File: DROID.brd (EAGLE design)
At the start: 160 x 100 mm, 83 parts

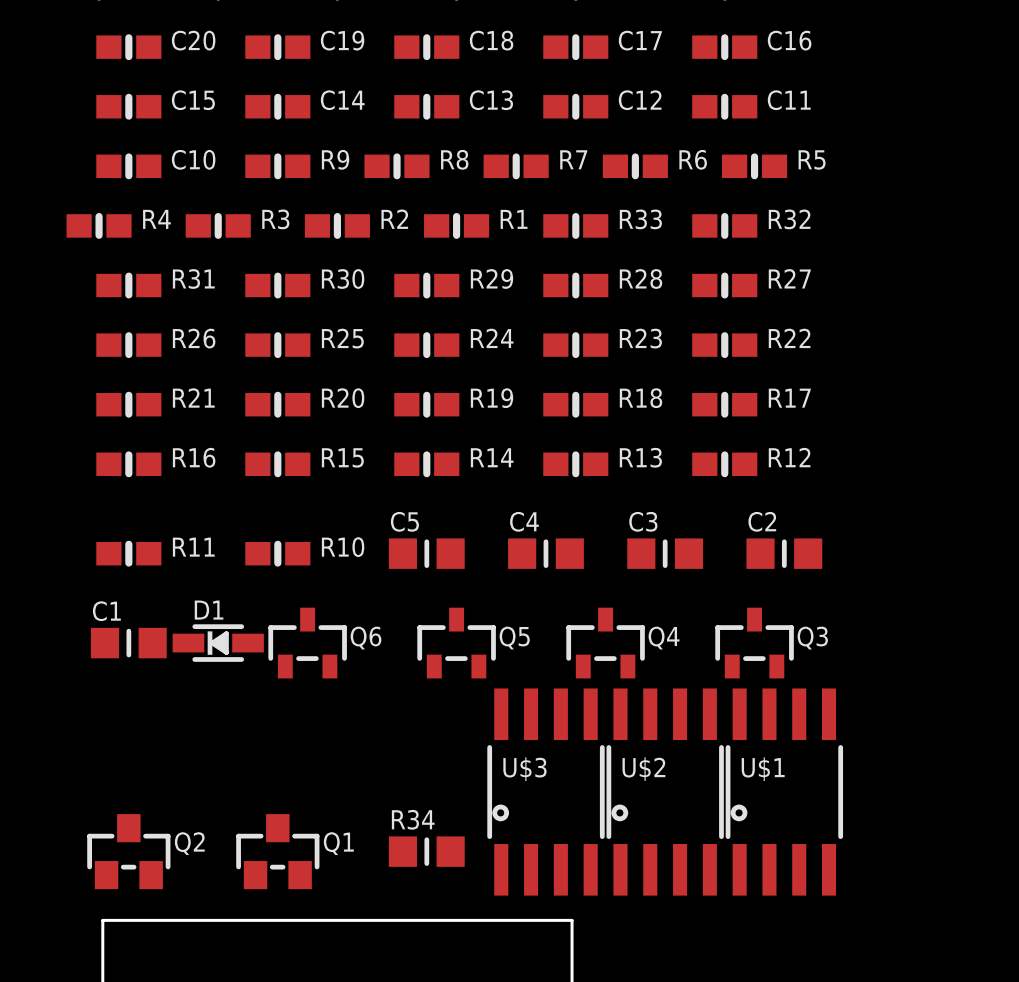
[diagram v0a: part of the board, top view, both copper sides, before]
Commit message: fixed passive names
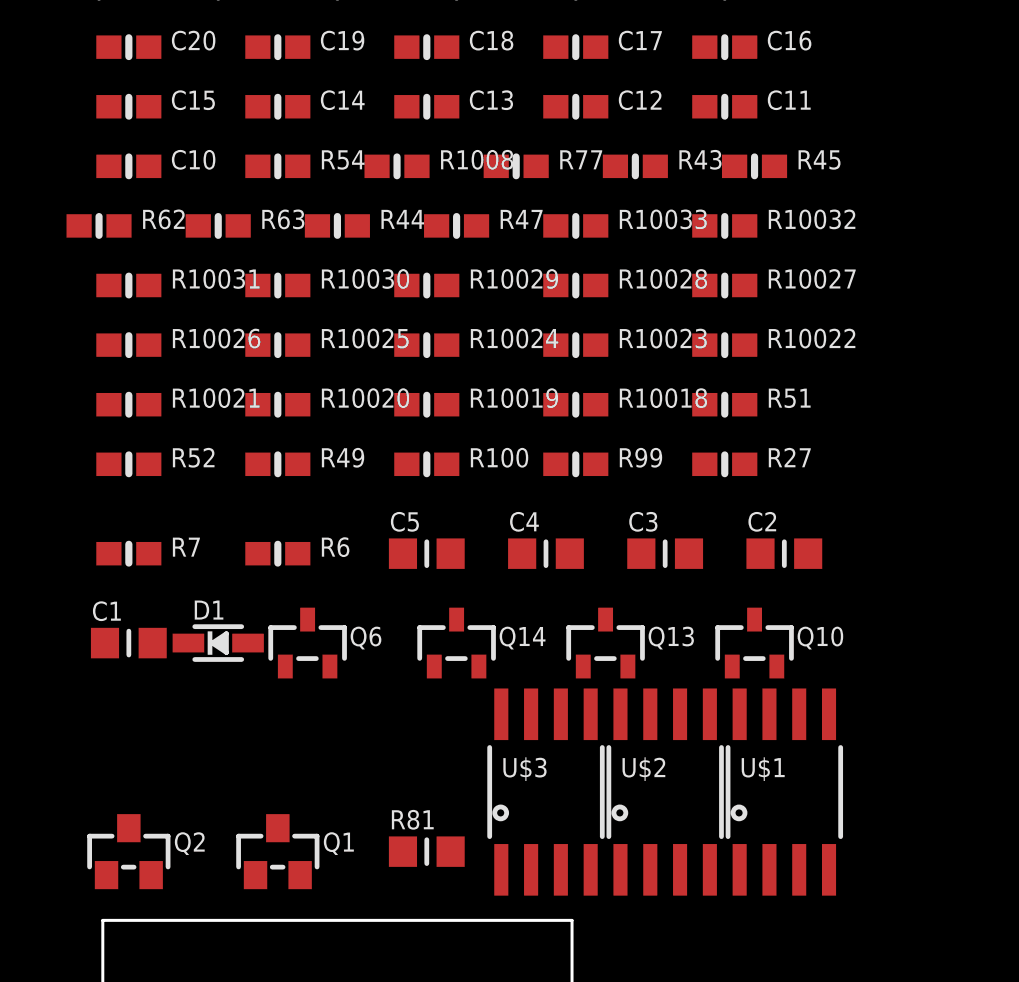
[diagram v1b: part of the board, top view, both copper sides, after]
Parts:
- removed R10, R11: 100, microbuilder:0603-NO
- removed R12: 1K, microbuilder:0603-NO
- added R10027: 100, microbuilder:0603-NO
- added R43: 100K, microbuilder:0603-NO
- added R77: 0, microbuilder:0603-NO
- R27: value 100 -> 1K
- R6: value 100K -> 100
- R7: value 0 -> 100
- moved R7 23.3 mm to (-43.2, 15.2)
- moved R6 22.5 mm to (-36.8, 15.2)
- moved R27 7.62 mm to (-17.8, 19.1)
- renumbered Q3 to Q10, Q4 to Q13, Q5 to Q14, R1 to R47, R13 to R99, R14 to R100, R15 to R49, R16 to R52, R17 to R51, R18 to R10018, R19 to R10019, R2 to R44, R20 to R10020, R21 to R10021, R22 to R10022, R23 to R10023, R24 to R10024, R25 to R10025, R26 to R10026, R28 to R10028, R29 to R10029, R3 to R63, R30 to R10030, R31 to R10031, R32 to R10032, R33 to R10033, R34 to R81, R4 to R62, R5 to R45, R8 to R1008, R9 to R54
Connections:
- removed net N$32 (its old number): R12.1
- removed net N$33 (its old number): R12.2
- removed net N$34 (its old number): R11.1
- removed net N$35 (its old number): R11.2
- removed net N$36 (its old number): R10.1
- removed net N$37 (its old number): R10.2
- new net N$111: R77.1
- new net N$112: R77.2
- new net N$127: R43.1
- new net N$128: R43.2
- new net N$85: R10027.1
- new net N$86: R10027.2

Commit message: more renames?
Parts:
- removed C1, C3: (no value), microbuilder:_0805MP
- removed C12, C6, C8: (no value), microbuilder:0603-NO
- added C23, C31, C33, C38: (no value), microbuilder:0603-NO
- C17, C19: device microbuilder:0603-NO -> microbuilder:_0805MP
- moved C19 26.2 mm to (-43.2, 11.4)
- moved C17 21.9 mm to (-20.3, 15.2)
- moved C16 21.7 mm to (-39.4, 39.4)
- moved C11 13.0 mm to (-30.5, 36.8)
- moved C18 2.84 mm to (-29.2, 39.4)
- moved C21 2.54 mm to (-17.8, 36.8)
- renumbered C10 to C35, C13 to C25, C14 to C24, C15 to C29, C2 to C28, C20 to C39, C22 to C26, C4 to C20A, C5 to C22A, C7 to C27, C9 to C36, Q1 to Q12, Q2 to Q11, R10018 to R25, R10019 to R71, R10020 to R68, R10021 to R26, R10022 to R76, R10023 to R59, R10024 to R61, R10025 to R55, R10026 to R60, R10027 to R29, R10028 to R23, R10029 to R18, R10030 to R22, R10031 to R66, R10032 to R64, R10033 to R5, R1008 to R30, R47 to R47_OR_42
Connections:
- removed net N$123 (its old number): C8.1
- removed net N$124 (its old number): C8.2
- removed net N$125 (its old number): C3.1
- removed net N$126 (its old number): C3.2
- removed net N$3 (its old number): C6.1
- removed net N$4 (its old number): C6.2
- removed net N$69: C12.1
- removed net N$7 (its old number): C1.1
- removed net N$70: C12.2
- removed net N$8 (its old number): C1.2
- new net N$51: C31.1
- new net N$52: C31.2
- new net N$55: C38.1
- new net N$56: C38.2
- new net N$57: C23.1
- new net N$58: C23.2
- new net N$71: C33.1
- new net N$72: C33.2

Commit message: renamed nets to make connections easier
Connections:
- net N$1 renamed C27_A
- net N$10 renamed R62_B
- net N$100 renamed R76_B
- net N$101 renamed R68_A
- net N$102 renamed R68_B
- net N$103 renamed R26_A
- net N$104 renamed R26_B
- net N$105 renamed R71_A
- net N$106 renamed R71_B
- net N$107 renamed R25_A
- net N$108 renamed R25_B
- net N$109 renamed R30_A
- net N$11 renamed R44_A
- net N$110 renamed R30_B
- net N$111 renamed R77_A
- net N$112 renamed R77_B
- net N$118 renamed C35_A
- net N$119 renamed C35_B
- net N$12 renamed R44_B
- net N$123 renamed C16_A
- net N$124 renamed C16_B
- net N$125 renamed C17_A
- net N$126 renamed C17_B
- net N$127 renamed R43_A
- net N$128 renamed R43_B
- net N$129 renamed R45_A
- net N$13 renamed R63_A
- net N$130 renamed R45_B
- net N$14 renamed R63_B
- net N$2 renamed C27_B
- net N$20 renamed R81_A
- net N$21 renamed R81_B
- net N$22 renamed R51_A
- net N$23 renamed R51_B
- net N$24 renamed R52_A
- net N$25 renamed R52_B
- net N$26 renamed R49_A
- net N$27 renamed R49_B
- net N$28 renamed R100_A
- net N$29 renamed R100_B
- net N$3 renamed C18_A
- net N$30 renamed R99_A
- net N$31 renamed R99_B
- net N$32 renamed R27_A
- net N$33 renamed R27_B
- net N$34 renamed R7_A
- net N$35 renamed R7_B
- net N$36 renamed R6_A
- net N$37 renamed R6_B
- net N$38 renamed R54_A
- net N$39 renamed R54_B
- net N$4 renamed C18_B
- net N$49 renamed C26_A
- net N$5 renamed C28_A
- net N$50 renamed C26_B
- net N$51 renamed C31_A
- net N$52 renamed C31_B
- net N$53 renamed C39_A
- net N$54 renamed C39_B
- net N$55 renamed C38_A
- net N$56 renamed C38_B
- net N$57 renamed C23_A
- net N$58 renamed C23_B
- net N$59 renamed C21_A
- net N$6 renamed C28_B
- net N$60 renamed C21_B
- net N$61 renamed C29_A
- net N$62 renamed C29_B
- net N$63 renamed C24_A
- net N$64 renamed C24_B
- net N$65 renamed C11_A
- net N$66 renamed C11_B
- net N$67 renamed C25_A
- net N$68 renamed C25_B
- net N$7 renamed C19_A
- net N$71 renamed C33_A
- net N$72 renamed C33_B
- net N$73 renamed R5_A
- net N$74 renamed R5_B
- net N$75 renamed R64_A
- net N$76 renamed R64_B
- net N$77 renamed C36_A
- net N$78 renamed C36_B
- net N$79 renamed R66_A
- net N$8 renamed C19_B
- net N$80 renamed R66_B
- net N$81 renamed R18_A
- net N$82 renamed R18_B
- net N$83 renamed R23_A
- net N$84 renamed R23_B
- net N$85 renamed R29_A
- net N$86 renamed R29_B
- net N$87 renamed R60_A
- net N$88 renamed R60_B
- net N$89 renamed R22_A
- net N$9 renamed R62_A
- net N$90 renamed R22_B
- net N$91 renamed R55_A
- net N$92 renamed R55_B
- net N$95 renamed R61_A
- net N$96 renamed R61_B
- net N$97 renamed R59_A
- net N$98 renamed R59_B
- net N$99 renamed R76_A
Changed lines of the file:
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@@
 </elements>
 <signals>
-<signal name="N$1">
+<signal name="C27_A">
 <contactref element="C27" pad="1"/>
 </signal>
-<signal name="N$2">
+<signal name="C27_B">
 <contactref element="C27" pad="2"/>
 </signal>
-<signal name="N$3">
+<signal name="C18_A">
 <contactref element="C18" pad="1"/>
 </signal>
-<signal name="N$4">
+<signal name="C18_B">
 <contactref element="C18" pad="2"/>
 </signal>
-<signal name="N$5">
+<signal name="C28_A">
 <contactref element="C28" pad="1"/>
 </signal>
-<signal name="N$6">
+<signal name="C28_B">
 <contactref element="C28" pad="2"/>
 </signal>
-<signal name="N$7">
+<signal name="C19_A">
 <contactref element="C19" pad="1"/>
 </signal>
-<signal name="N$8">
+<signal name="C19_B">
 <contactref element="C19" pad="2"/>
 </signal>
-<signal name="N$9">
+<signal name="R62_A">
 <contactref element="R62" pad="1"/>
 </signal>
-<signal name="N$10">
+<signal name="R62_B">
 <contactref element="R62" pad="2"/>
 </signal>
-<signal name="N$11">
+<signal name="R44_A">
 <contactref element="R44" pad="1"/>
 </signal>
-<signal name="N$12">
+<signal name="R44_B">
 <contactref element="R44" pad="2"/>
 </signal>
-<signal name="N$13">
+<signal name="R63_A">
 <contactref element="R63" pad="1"/>
 </signal>
-<signal name="N$14">
+<signal name="R63_B">
 <contactref element="R63" pad="2"/>
 </signal>
@@
 <contactref element="Q14" pad="2"/>
 </signal>
-<signal name="N$20">
+<signal name="R81_A">
 <contactref element="R81" pad="1"/>
 </signal>
-<signal name="N$21">
+<signal name="R81_B">
 <contactref element="R81" pad="2"/>
 </signal>
-<signal name="N$22">
+<signal name="R51_A">
 <contactref element="R51" pad="1"/>
 </signal>
-<signal name="N$23">
+<signal name="R51_B">
 <contactref element="R51" pad="2"/>
 </signal>
-<signal name="N$24">
+<signal name="R52_A">
 <contactref element="R52" pad="1"/>
 </signal>
-<signal name="N$25">
+<signal name="R52_B">
 <contactref element="R52" pad="2"/>
 </signal>
-<signal name="N$26">
+<signal name="R49_A">
 <contactref element="R49" pad="1"/>
 </signal>
-<signal name="N$27">
+<signal name="R49_B">
 <contactref element="R49" pad="2"/>
 </signal>
-<signal name="N$28">
+<signal name="R100_A">
 <contactref element="R100" pad="1"/>
 </signal>
-<signal name="N$29">
+<signal name="R100_B">
 <contactref element="R100" pad="2"/>
 </signal>
-<signal name="N$30">
+<signal name="R99_A">
 <contactref element="R99" pad="1"/>
 </signal>
-<signal name="N$31">
+<signal name="R99_B">
 <contactref element="R99" pad="2"/>
 </signal>
-<signal name="N$32">
+<signal name="R27_A">
 <contactref element="R27" pad="1"/>
 </signal>
-<signal name="N$33">
+<signal name="R27_B">
 <contactref element="R27" pad="2"/>
 </signal>
-<signal name="N$34">
+<signal name="R7_A">
 <contactref element="R7" pad="1"/>
 </signal>
-<signal name="N$35">
+<signal name="R7_B">
 <contactref element="R7" pad="2"/>
 </signal>
-<signal name="N$36">
+<signal name="R6_A">
 <contactref element="R6" pad="1"/>
 </signal>
-<signal name="N$37">
+<signal name="R6_B">
 <contactref element="R6" pad="2"/>
 </signal>
-<signal name="N$38">
+<signal name="R54_A">
 <contactref element="R54" pad="1"/>
 </signal>
-<signal name="N$39">
+<signal name="R54_B">
 <contactref element="R54" pad="2"/>
 </signal>
@@
 <contactref element="Q10" pad="2"/>
 </signal>
-<signal name="N$49">
+<signal name="C26_A">
 <contactref element="C26" pad="1"/>
 </signal>
-<signal name="N$50">
+<signal name="C26_B">
 <contactref element="C26" pad="2"/>
 </signal>
-<signal name="N$51">
+<signal name="C31_A">
 <contactref element="C31" pad="1"/>
 </signal>
-<signal name="N$52">
+<signal name="C31_B">
 <contactref element="C31" pad="2"/>
 </signal>
-<signal name="N$53">
+<signal name="C39_A">
 <contactref element="C39" pad="1"/>
 </signal>
-<signal name="N$54">
+<signal name="C39_B">
 <contactref element="C39" pad="2"/>
 </signal>
-<signal name="N$55">
+<signal name="C38_A">
 <contactref element="C38" pad="1"/>
 </signal>
-<signal name="N$56">
+<signal name="C38_B">
 <contactref element="C38" pad="2"/>
 </signal>
-<signal name="N$57">
+<signal name="C23_A">
 <contactref element="C23" pad="1"/>
 </signal>
-<signal name="N$58">
+<signal name="C23_B">
 <contactref element="C23" pad="2"/>
 </signal>
-<signal name="N$59">
+<signal name="C21_A">
 <contactref element="C21" pad="1"/>
 </signal>
-<signal name="N$60">
+<signal name="C21_B">
 <contactref element="C21" pad="2"/>
 </signal>
-<signal name="N$61">
+<signal name="C29_A">
 <contactref element="C29" pad="1"/>
 </signal>
-<signal name="N$62">
+<signal name="C29_B">
 <contactref element="C29" pad="2"/>
 </signal>
-<signal name="N$63">
+<signal name="C24_A">
 <contactref element="C24" pad="1"/>
 </signal>
-<signal name="N$64">
+<signal name="C24_B">
 <contactref element="C24" pad="2"/>
 </signal>
-<signal name="N$65">
+<signal name="C11_A">
 <contactref element="C11" pad="1"/>
 </signal>
-<signal name="N$66">
+<signal name="C11_B">
 <contactref element="C11" pad="2"/>
 </signal>
-<signal name="N$67">
+<signal name="C25_A">
 <contactref element="C25" pad="1"/>
 </signal>
-<signal name="N$68">
+<signal name="C25_B">
 <contactref element="C25" pad="2"/>
 </signal>
-<signal name="N$71">
+<signal name="C33_A">
 <contactref element="C33" pad="1"/>
 </signal>
-<signal name="N$72">
+<signal name="C33_B">
 <contactref element="C33" pad="2"/>
 </signal>
-<signal name="N$73">
+<signal name="R5_A">
 <contactref element="R5" pad="1"/>
 </signal>
-<signal name="N$74">
+<signal name="R5_B">
 <contactref element="R5" pad="2"/>
 </signal>
-<signal name="N$75">
+<signal name="R64_A">
 <contactref element="R64" pad="1"/>
 </signal>
-<signal name="N$76">
+<signal name="R64_B">
 <contactref element="R64" pad="2"/>
 </signal>
-<signal name="N$77">
+<signal name="C36_A">
 <contactref element="C36" pad="1"/>
 </signal>
-<signal name="N$78">
+<signal name="C36_B">
 <contactref element="C36" pad="2"/>
 </signal>
-<signal name="N$79">
+<signal name="R66_A">
 <contactref element="R66" pad="1"/>
 </signal>
-<signal name="N$80">
+<signal name="R66_B">
 <contactref element="R66" pad="2"/>
 </signal>
-<signal name="N$81">
+<signal name="R18_A">
 <contactref element="R18" pad="1"/>
 </signal>
-<signal name="N$82">
+<signal name="R18_B">
 <contactref element="R18" pad="2"/>
 </signal>
-<signal name="N$83">
+<signal name="R23_A">
 <contactref element="R23" pad="1"/>
 </signal>
-<signal name="N$84">
+<signal name="R23_B">
 <contactref element="R23" pad="2"/>
 </signal>
-<signal name="N$85">
+<signal name="R29_A">
 <contactref element="R29" pad="1"/>
 </signal>
-<signal name="N$86">
+<signal name="R29_B">
 <contactref element="R29" pad="2"/>
 </signal>
-<signal name="N$87">
+<signal name="R60_A">
 <contactref element="R60" pad="1"/>
 </signal>
-<signal name="N$88">
+<signal name="R60_B">
 <contactref element="R60" pad="2"/>
 </signal>
-<signal name="N$89">
+<signal name="R22_A">
 <contactref element="R22" pad="1"/>
 </signal>
-<signal name="N$90">
+<signal name="R22_B">
 <contactref element="R22" pad="2"/>
 </signal>
-<signal name="N$91">
+<signal name="R55_A">
 <contactref element="R55" pad="1"/>
 </signal>
-<signal name="N$92">
+<signal name="R55_B">
 <contactref element="R55" pad="2"/>
 </signal>
@@
 <contactref element="C20A" pad="2"/>
 </signal>
-<signal name="N$95">
+<signal name="R61_A">
 <contactref element="R61" pad="1"/>
 </signal>
-<signal name="N$96">
+<signal name="R61_B">
 <contactref element="R61" pad="2"/>
 </signal>
-<signal name="N$97">
+<signal name="R59_A">
 <contactref element="R59" pad="1"/>
 </signal>
-<signal name="N$98">
+<signal name="R59_B">
 <contactref element="R59" pad="2"/>
 </signal>
-<signal name="N$99">
+<signal name="R76_A">
 <contactref element="R76" pad="1"/>
 </signal>
-<signal name="N$100">
+<signal name="R76_B">
 <contactref element="R76" pad="2"/>
 </signal>
-<signal name="N$101">
+<signal name="R68_A">
 <contactref element="R68" pad="1"/>
 </signal>
-<signal name="N$102">
+<signal name="R68_B">
 <contactref element="R68" pad="2"/>
 </signal>
-<signal name="N$103">
+<signal name="R26_A">
 <contactref element="R26" pad="1"/>
 </signal>
-<signal name="N$104">
+<signal name="R26_B">
 <contactref element="R26" pad="2"/>
 </signal>
-<signal name="N$105">
+<signal name="R71_A">
 <contactref element="R71" pad="1"/>
 </signal>
-<signal name="N$106">
+<signal name="R71_B">
 <contactref element="R71" pad="2"/>
 </signal>
-<signal name="N$107">
+<signal name="R25_A">
 <contactref element="R25" pad="1"/>
 </signal>
-<signal name="N$108">
+<signal name="R25_B">
 <contactref element="R25" pad="2"/>
 </signal>
-<signal name="N$109">
+<signal name="R30_A">
 <contactref element="R30" pad="1"/>
 </signal>
-<signal name="N$110">
+<signal name="R30_B">
 <contactref element="R30" pad="2"/>
 </signal>
-<signal name="N$111">
+<signal name="R77_A">
 <contactref element="R77" pad="1"/>
 </signal>
-<signal name="N$112">
+<signal name="R77_B">
 <contactref element="R77" pad="2"/>
 </signal>
@@
 <contactref element="Q11" pad="3"/>
 </signal>
-<signal name="N$118">
+<signal name="C35_A">
 <contactref element="C35" pad="1"/>
 </signal>
-<signal name="N$119">
+<signal name="C35_B">
 <contactref element="C35" pad="2"/>
 </signal>
@@
 <contactref element="Q12" pad="3"/>
 </signal>
-<signal name="N$123">
+<signal name="C16_A">
 <contactref element="C16" pad="1"/>
 </signal>
-<signal name="N$124">
+<signal name="C16_B">
 <contactref element="C16" pad="2"/>
 </signal>
-<signal name="N$125">
+<signal name="C17_A">
 <contactref element="C17" pad="1"/>
 </signal>
-<signal name="N$126">
+<signal name="C17_B">
 <contactref element="C17" pad="2"/>
 </signal>
-<signal name="N$127">
+<signal name="R43_A">
 <contactref element="R43" pad="1"/>
 </signal>
-<signal name="N$128">
+<signal name="R43_B">
 <contactref element="R43" pad="2"/>
 </signal>
-<signal name="N$129">
+<signal name="R45_A">
 <contactref element="R45" pad="1"/>
 </signal>
-<signal name="N$130">
+<signal name="R45_B">
 <contactref element="R45" pad="2"/>
 </signal>

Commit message: net name/connection updates
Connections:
- net LED- renamed PAIR_LED-
- net N$115 renamed Q11_B
- net N$116 renamed Q11_E
- net N$117 renamed Q11_C
- net N$120 renamed Q12_B
- net N$121 renamed Q12_E
- net N$131 renamed HEAD_OUT_B
- net N$132 renamed HEAD_OUT_A
- net N$139 renamed RIGHT_OUT_B
- net N$140 renamed RIGHT_OUT_A
- net N$141 renamed RIGHT_IN_B
- net N$142 renamed RIGHT_IN_A
- net N$147 renamed LEFT_OUT_B
- net N$148 renamed LEFT_OUT_A
- net N$17 renamed Q14_B
- net N$18 renamed Q14_C
- net N$19 renamed Q14_E
- net N$40 renamed Q6_B
- net N$41 renamed Q6_C
- net N$42 renamed Q6_E
- net N$43 renamed Q13_B
- net N$44 renamed Q13_C
- net N$45 renamed Q13_E
- net N$46 renamed Q10_B
- net N$47 renamed Q10_C
- net N$48 renamed Q10_E
- removed net LED+: JP11.3
- removed net N$122: Q12.3
- removed net N$133: U$3.3
- removed net N$134: U$3.1
- removed net N$149: U$1.3
- removed net N$150: U$1.1
- removed net P0.00: U$4.P$11
- removed net P0.1: U$4.P$12
- removed net P0.10: U$4.P$21
- removed net P0.11: U$4.P$22
- removed net P0.12: U$4.P$23
- removed net P0.13: U$4.P$24
- removed net P0.16: U$4.P$27
- removed net P0.2: U$4.P$13
- removed net P0.20: U$4.P$31
- removed net P0.21: U$4.P$1
- removed net P0.22: U$4.P$2
- removed net P0.23: U$4.P$3
- removed net P0.24: U$4.P$4
- removed net P0.25: U$4.P$5
- removed net P0.26: U$4.P$6
- removed net P0.27: U$4.P$7
- removed net P0.28: U$4.P$8
- removed net P0.29: U$4.P$9
- removed net P0.3: U$4.P$14
- removed net P0.30: U$4.P$10
- removed net P0.4: U$4.P$15
- removed net P0.5: U$4.P$16
- removed net P0.6: U$4.P$17
- removed net P0.7: U$4.P$18
- removed net P0.8: U$4.P$19
- removed net P0.9: U$4.P$20
- removed net PAIR: JP11.1
- removed net Q12_COL: U$5.5
- removed net R100: U$5.15
- removed net R25: U$5.6
- removed net R27: U$5.9
- removed net R99: U$5.14
- new net HEAD_IN_A: U$3.1, U$4.P$3
- new net HEAD_IN_B: U$3.3, U$4.P$4
- new net LEFT_IN_A: U$1.1, U$4.P$5
- new net LEFT_IN_B: U$1.3, U$4.P$10
- new net PAIR_BTN: JP11.1, U$4.P$24
- new net PAIR_LED+: JP11.3, U$4.P$22
- new net Q12_C: Q12.3, U$5.5
- net GND: now also U$4.P$9
- net R100_B: now also U$5.15
- net R22_B: now also U$4.P$12
- net R23_B: now also U$4.P$16
- net R25_B: now also U$5.6
- net R27_B: now also U$5.9
- net R29_B: now also U$4.P$15
- net R49_B: now also U$4.P$13
- net R51_B: now also U$4.P$2
- net R52_B: now also U$4.P$18
- net R55_B: now also U$4.P$14
- net R62_B: now also U$4.P$19
- net R63_B: now also U$4.P$20
- net R64_B: now also U$4.P$23
- net R99_B: now also U$5.14
- net SWCLK: now also U$4.P$27
- net SWDIO: now also U$4.P$31
- net VCC_3: now also U$4.P$11
- net VCC_33: now also U$4.P$8
